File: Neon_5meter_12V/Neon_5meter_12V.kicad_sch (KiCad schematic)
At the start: 44 parts, among them J1 Conn_01x16_Pin, J2 +12V Jack, J3 Conn_01x16_Pin, J4 Blue strip jack, J5 Pink strip Jack, J6 Conn_01x03_Pin, Q1 IRLML2502TRPBF, Q2 IRLML2502TRPBF, Q3 BSS138, Q4 BSS138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

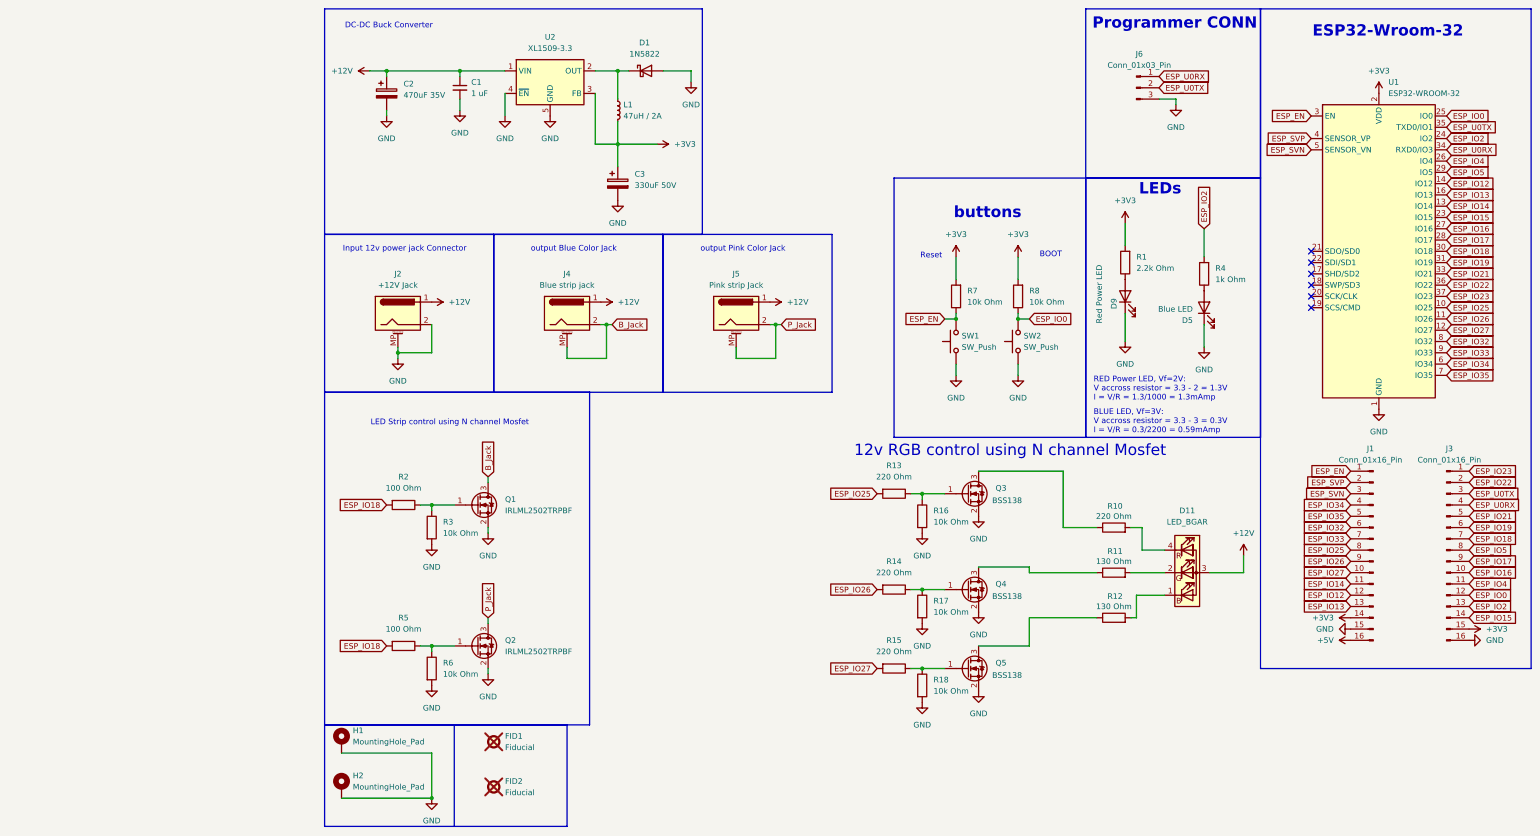
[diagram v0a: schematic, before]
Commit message: updated RGB 5mm led current sensing resistors values for 12v supply on anode
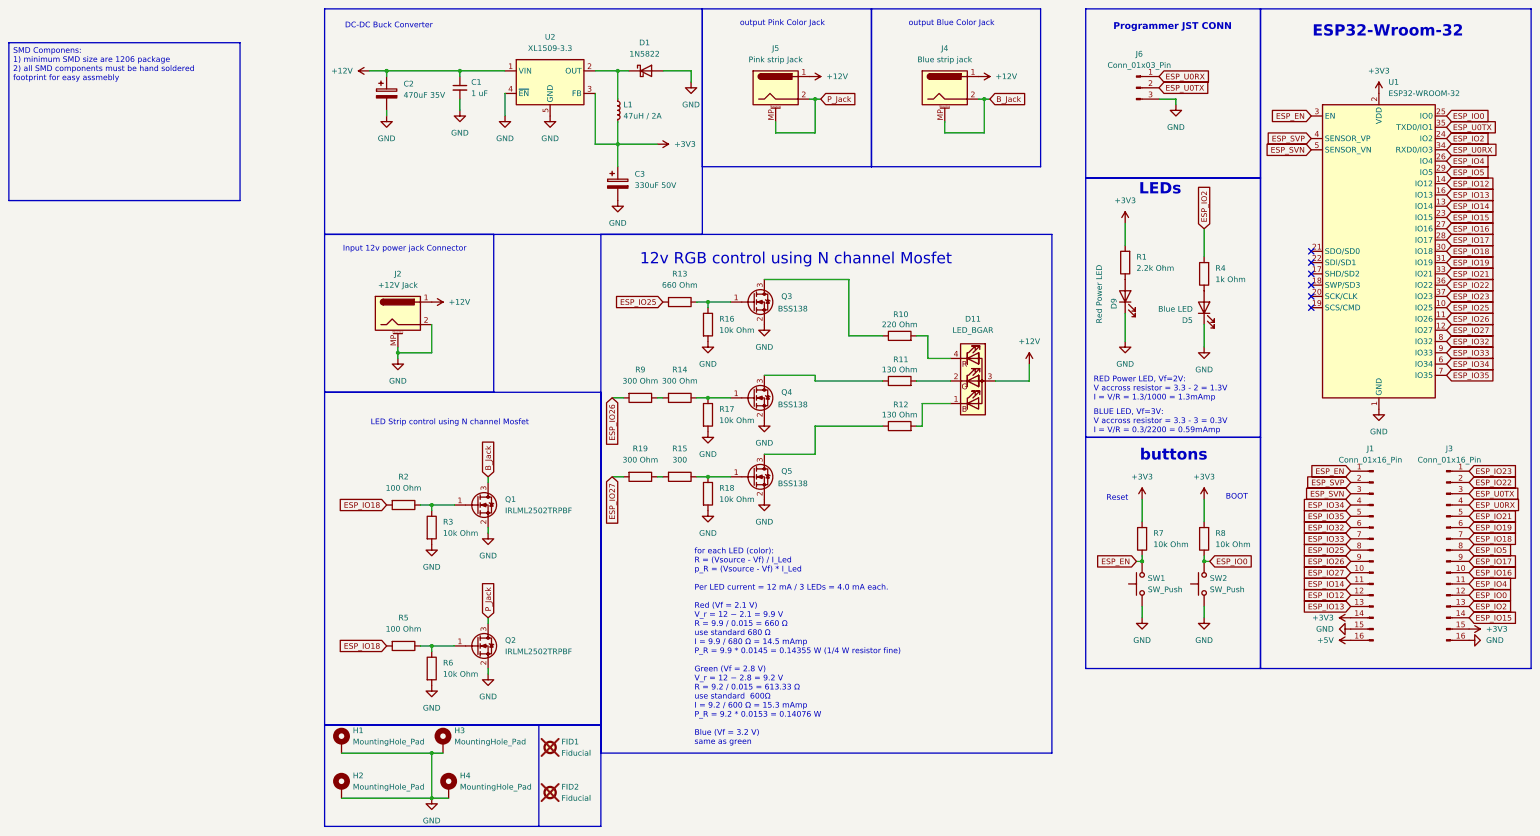
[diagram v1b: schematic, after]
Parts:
- added H3, H4: MountingHole_Pad, MountingHole:MountingHole_3.2mm_M3_Pad_Via, symbol Mechanical:MountingHole_Pad
- added R19, R9: 300 Ohm, Resistor_SMD:R_1206_3216Metric_Pad1.30x1.75mm_HandSolder, symbol Device:R
- R13: value 220 Ohm -> 660 Ohm; link https://uge-one.com/product/smd-chip-resistor-size-1206-220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 -> https://makerselectronics.com/product/chip-resistor-smd-680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
- R14: value 220 Ohm -> 300 Ohm; link https://uge-one.com/product/smd-chip-resistor-size-1206-220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 -> https://uge-one.com/product/smd-chip-resistor-size-1206-300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
- R15: value 220 Ohm -> 300; link https://uge-one.com/product/smd-chip-resistor-size-1206-220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 -> https://uge-one.com/product/smd-chip-resistor-size-1206-300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
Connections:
- net ESP_IO26: now also R9.2; no longer R14.2
- net ESP_IO27: now also R19.2; no longer R15.2
- net GND: now also H3.1, H4.1
- new net: R15.2, R19.1
- new net: R14.2, R9.1
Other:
- note added: "Programmer JST CONN"
- note added: "for each LED (color): R = (Vsource - Vf) / I_Led p_R = (Vsource - Vf) * I_Led Per LED current = 12 mA / 3 LEDs = 4.0 mA each. Red (Vf = 2.1 V) V_r = 12 − 2.1 = 9.9 V R = 9.9 / 0.015 = 660 Ω use standard 680 Ω I = 9.9 / 680 Ω = 14.5 mAmp P_R = 9.9 * 0.0145 = 0.14355 W (1/4 W resistor fine) Green (Vf = 2.8 V) V_r = 12 − 2.8 = 9.2 V R = 9.2 / 0.015 = 613.33 Ω use standard 600Ω I = 9.2 / 600 Ω = 15.3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"
- note removed: "Programmer CONN"
- title: Neon 5meter 12V -> Neon 1meter 12V
- moved on the sheet: D11, FID1, FID2, J4, J5, Q3, Q4, Q5, R10, R11, R12, R13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

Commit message: updated errors
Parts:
- R11, R12: value 130 Ohm -> 220 Ohm; link https://makerselectronics.com/product/chip-resistor-smd-130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 -> https://uge-one.com/product/smd-chip-resistor-size-1206-220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
- R15: value 300 -> 300 Ohm
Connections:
- net ESP_IO25: now also R10.2; no longer R13.2
- net ESP_IO26: now also R11.2; no longer R9.2
- net ESP_IO27: now also R12.2; no longer R19.2
- net at Q3.1 (G), R16.1: now also R10.1; no longer R13.1
- net at R11.1: now also Q4.1 (G), R17.1; no longer Q4.3 (D)
- net at D11.2 (GK): now also R14.1; no longer R11.2
- net at R12.1: now also Q5.1 (G), R18.1; no longer Q5.3 (D)
- net at D11.1 (BK): now also R15.1; no longer R12.2
- net at Q3.3 (D): now also R13.2; no longer R10.1
- net at D11.4 (RK): now also R13.1; no longer R10.2
- new net: Q5.3 (D), R19.2
- new net: Q4.3 (D), R9.2
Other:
- moved on the sheet: R13, R14, R15, R19, R9
